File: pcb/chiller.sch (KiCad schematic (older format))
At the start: 41 parts, among them J1 CONN_01X03, J10 CONN_01X03, J11 CONN_01X02, J12 CONN_01X02, J2 CONN_01X03, J3 CONN_01X03, J4 CONN_01X02, J5 CONN_01X02, J6 CONN_01X02, J7 CONN_01X02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

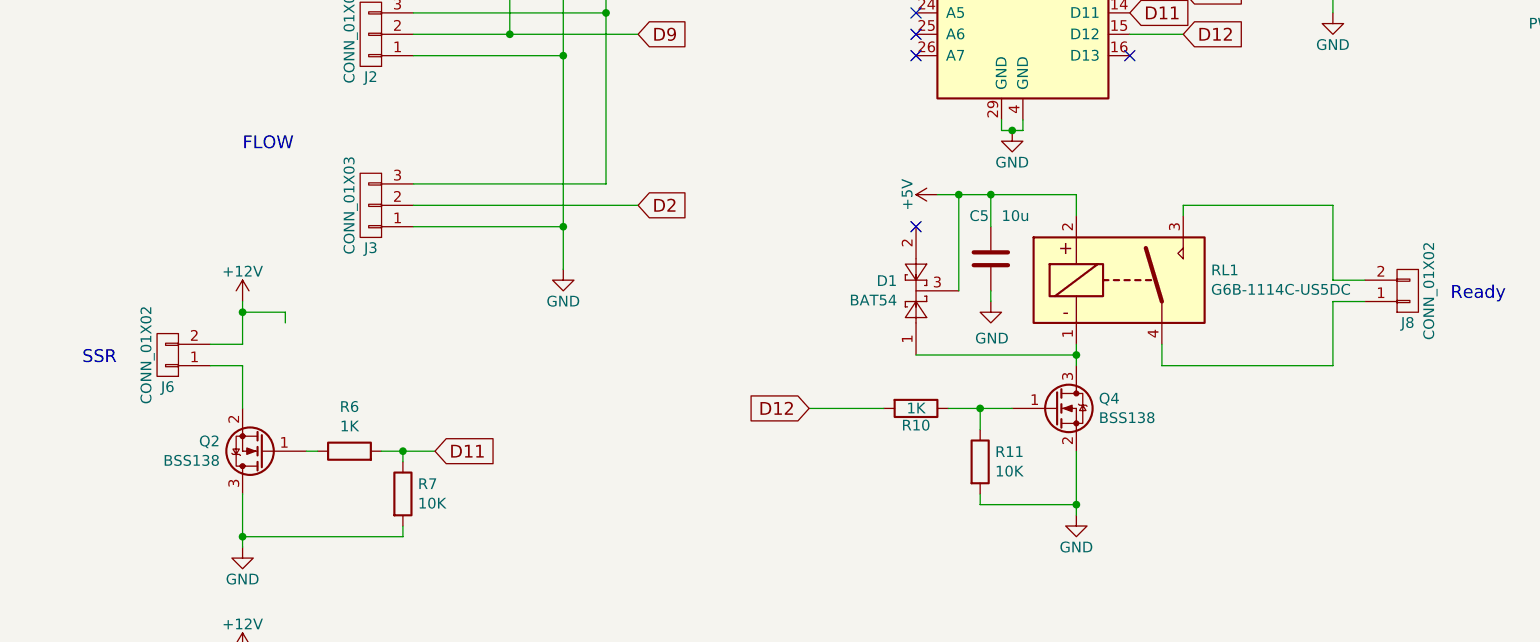
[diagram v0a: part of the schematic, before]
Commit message: Fix errors: - Relay wrong footprint - Q2 switched D and G
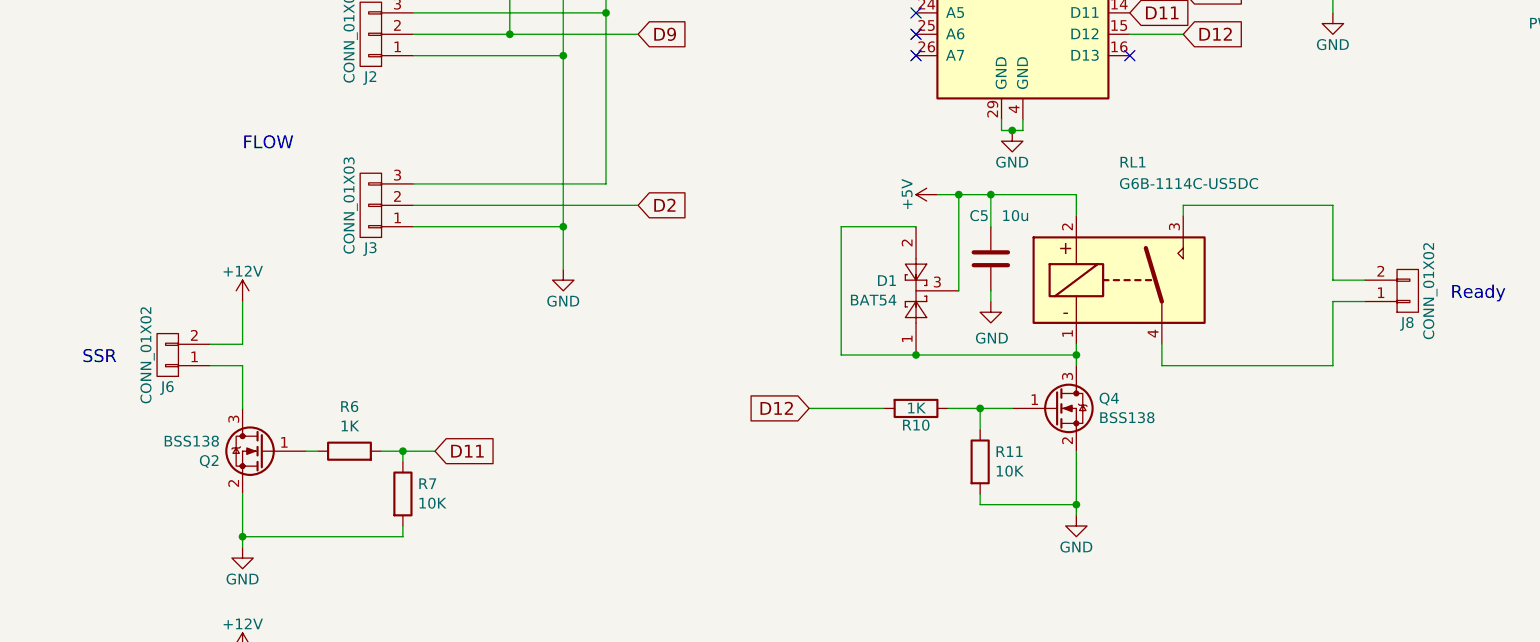
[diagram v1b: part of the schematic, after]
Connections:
- net GND: now also Q2.2 (S); no longer Q2.3 (D)
- net at J6.1 (P1): now also Q2.3 (D); no longer Q2.2 (S)
- net at D1.1, Q4.3 (D), RL1.1: now also D1.2
- no-connect marks 16 -> 15
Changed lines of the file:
@@
 $EndComp
-Wire Wire Line
-	3700 4500 3700 4550
 Wire Wire Line
 	3700 4700 3550 4700
@@
 Wire Wire Line
 	7050 4000 7050 4450
-NoConn ~ 6850 4150
 $Comp
 L Transistor_FET:BSS138 Q2
@@
 F 3 "https://www.fairchildsemi.com/datasheets/BS/BSS138.pdf" H 3800 5200 50  0001 L CNN
 	1    3800 5200
-	-1   0    0    1
+	-1   0    0    -1
 $EndComp
 $Comp
@@
 $EndComp
 Wire Wire Line
-	3900 4600 3900 4550
-Wire Wire Line
-	3900 4550 3700 4550
-Connection ~ 3700 4550
-Wire Wire Line
-	3700 4550 3700 4700
-Wire Wire Line
 	3850 6550 3850 6600
 Wire Wire Line
@@
 U 1 1 5BCAFCFB
 P 7800 4400
-F 0 "RL1" H 8230 4446 50  0000 L CNN
-F 1 "G6B-1114C-US5DC" H 8230 4355 50  0000 L CNN
+F 0 "RL1" H 7800 4950 50  0000 L CNN
+F 1 "G6B-1114C-US5DC" H 7800 4850 50  0000 L CNN
 F 2 "modules:DIL-relay" H 7800 4400 50  0001 C CNN
 F 3 "" H 7800 4400 50  0001 C CNN
@@
 	1    0    0    -1
 $EndComp
+Wire Wire Line
+	6850 4150 6500 4150
+Wire Wire Line
+	6500 4150 6500 4750
+Wire Wire Line
+	6500 4750 6850 4750
+Connection ~ 6850 4750
+Wire Wire Line
+	3700 4500 3700 4700
 $EndSCHEMATC
